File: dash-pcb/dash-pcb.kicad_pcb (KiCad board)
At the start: 2 copper layers, 86.4 x 94 mm, 17 parts, among them U2 Teensy2.0_(Arduino)

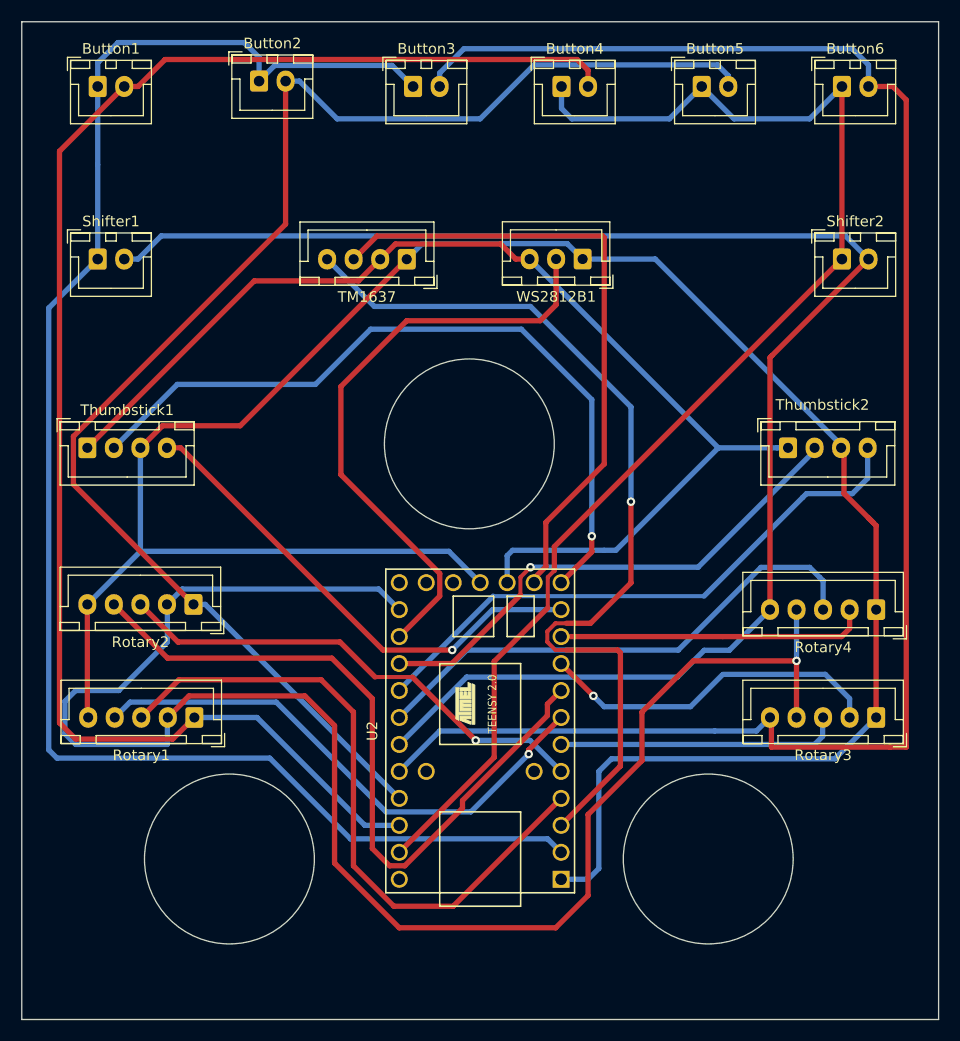
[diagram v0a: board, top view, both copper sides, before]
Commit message: fixed thumbstick 1 analogic pin
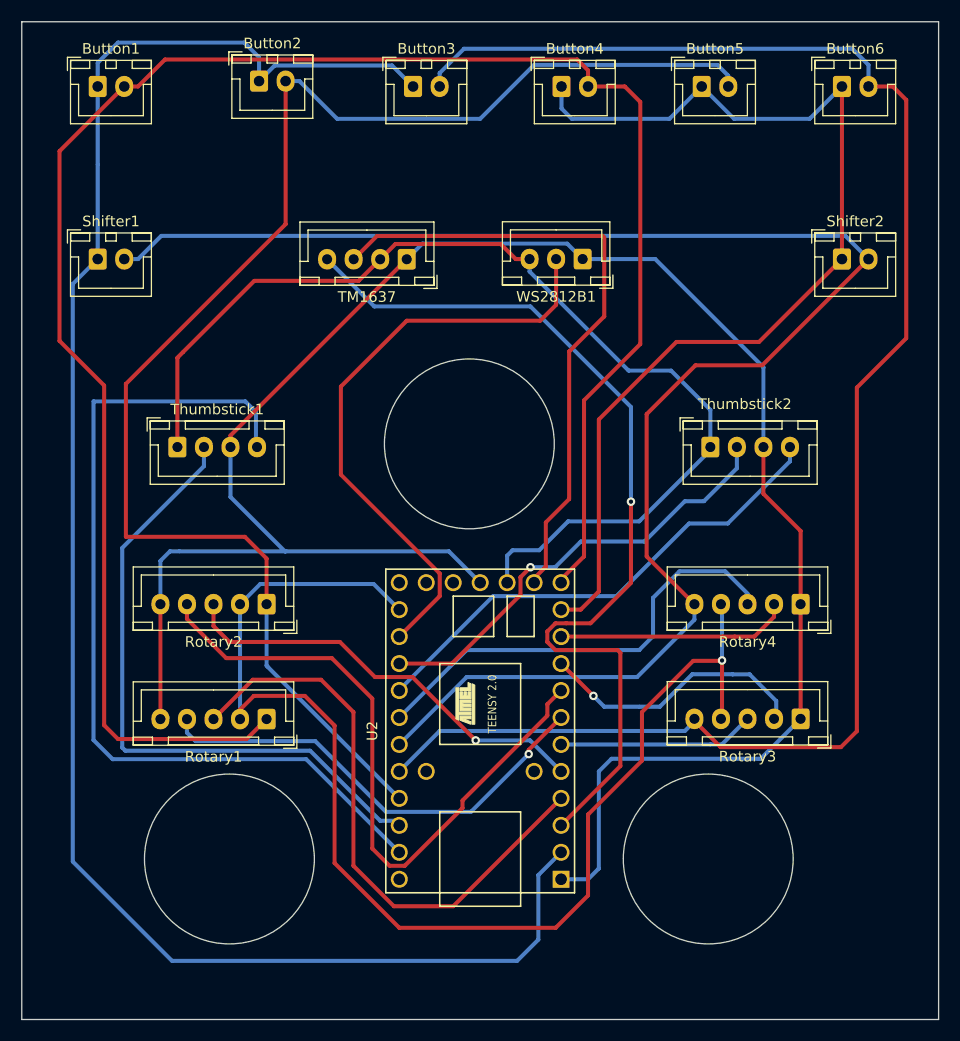
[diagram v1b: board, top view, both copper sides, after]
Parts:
- moved Thumbstick1 8.48 mm to (118.8, 68.0)
- moved Thumbstick2 7.32 mm to (169.0, 68.0)
- moved Rotary4 7.14 mm to (177.5, 82.8)
- moved Rotary3 7.12 mm to (177.5, 93.6)
- moved Rotary2 6.88 mm to (127.2, 82.8)
- moved Rotary1 6.81 mm to (127.2, 93.6)
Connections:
- U2 pad 11: Net-(Thumbstick1-Pin_4) -> Net-(Button4-Pin_1)
- U2 pad 12: Net-(Thumbstick1-Pin_2) -> Net-(Button1-Pin_2)
- U2 pad 27: Net-(Button1-Pin_2) -> Net-(Thumbstick1-Pin_2)
- U2 pad 28: Net-(Button4-Pin_1) -> Net-(Thumbstick1-Pin_4)
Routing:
- net Net-(Rotary1-Pin_2): track 158.9 -> 119.5 mm
- net Net-(Thumbstick1-Pin_4): track 46.6 -> 84.1 mm, vias 1 -> 0
- net Net-(Button1-Pin_2): track 146.8 -> 181.6 mm
- net Net-(Button4-Pin_1): track 122.1 -> 98.6 mm
- net GND: track 211.6 -> 191.1 mm
- net Net-(Button1-Pin_1): track 153.6 -> 168.6 mm
- net Net-(Thumbstick1-Pin_2): track 70.8 -> 60.6 mm, vias 1 -> 0
- net +5V: track 108.8 -> 99.8 mm
- net Net-(Rotary3-Pin_3): track 26.7 -> 18.6 mm
- net Net-(Thumbstick2-Pin_4): track 55.3 -> 47.1 mm
- net Net-(Rotary1-Pin_4): track 50.8 -> 43.5 mm
- net Net-(Rotary4-Pin_2): track 29.3 -> 22.0 mm
- net Net-(Rotary1-Pin_3): track 62.5 -> 55.8 mm
- net Net-(Rotary3-Pin_2): track 32.7 -> 26.1 mm
- net Net-(Rotary4-Pin_3): track 49.0 -> 42.5 mm
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
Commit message: improved tracks
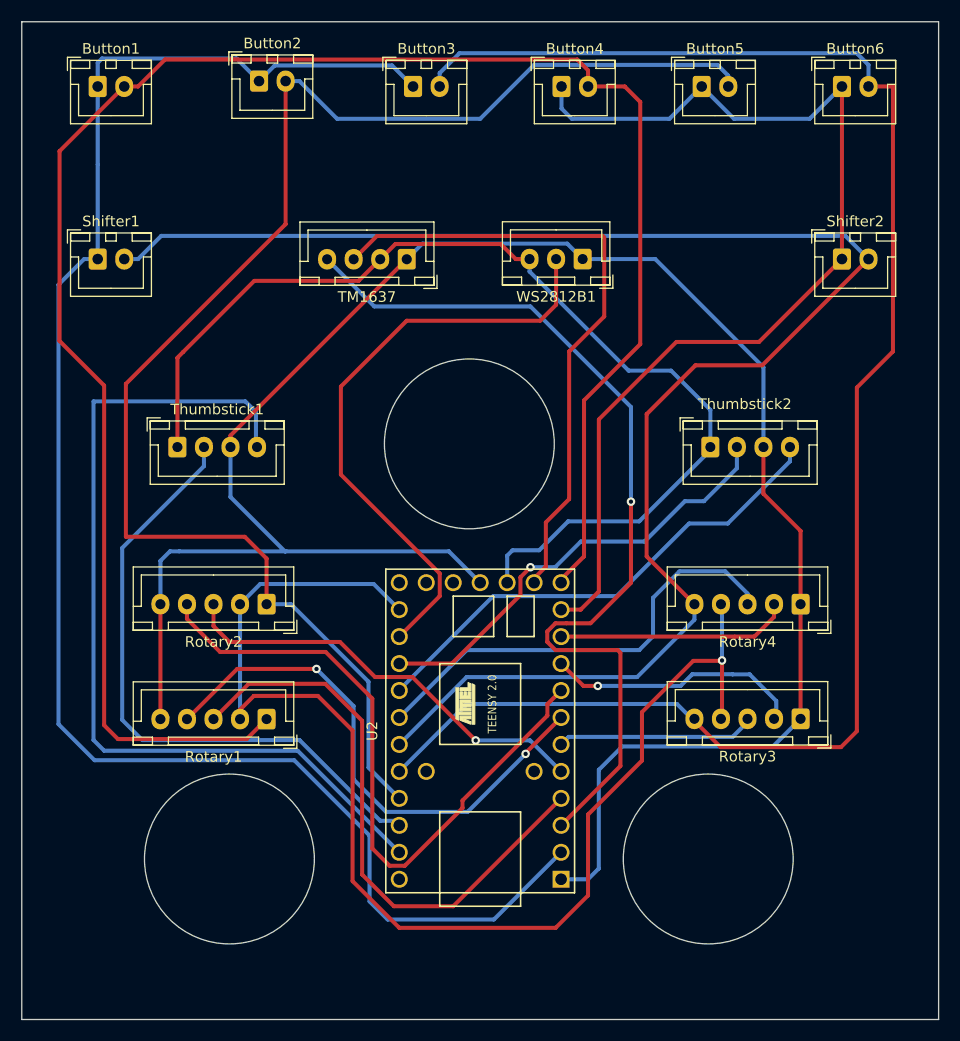
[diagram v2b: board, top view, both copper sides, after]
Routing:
- net Net-(Button1-Pin_1): track 168.6 -> 158.0 mm
- net Net-(Rotary1-Pin_4): track 43.5 -> 50.6 mm, vias 1 -> 2
- net Net-(Rotary3-Pin_2): track 26.1 -> 24.5 mm
- net Net-(Thumbstick1-Pin_2): track 60.6 -> 59.1 mm
- net Net-(Button2-Pin_2): track 137.7 -> 139.1 mm
- net Net-(Rotary1-Pin_2): track 119.5 -> 120.2 mm
